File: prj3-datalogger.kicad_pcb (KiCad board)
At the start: 2 copper layers, 29 parts, among them J1 Conn_01x04_Pin, J2 Conn_01x04_Pin, J3 Conn_01x09_Pin, J4 Conn_02x03_Odd_Even, U1 24LC1025, U2 24LC1025, U3 DS1337S_, U4 ATMEGA328P-AU, Y1 32.768 KHz, Y2 16 MHz

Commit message: complet placement of comps.
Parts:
- moved J3 93.8 mm to (81.5, 106.7), turned to 90 degrees
- moved Y1 87.6 mm to (75.9, 95.6), turned to 90 degrees
- moved C1 71.6 mm to (92.7, 80.4)
- moved J1 71.5 mm to (109.1, 106.7), turned to 90 degrees
- moved C4 70.3 mm to (91.9, 101.1), turned to -90 degrees
- moved H4 69.1 mm to (75.3, 80.0)
- moved U3 68.9 mm to (84.8, 100.0)
- moved C3 68.6 mm to (97.8, 80.4)
- moved U1 68.2 mm to (84.7, 82.1)
- moved U2 68.0 mm to (84.7, 90.9)
- moved H3 65.3 mm to (75.3, 106.8)
- moved C2 63.1 mm to (102.5, 80.5), turned to 180 degrees
- moved Y2 62.9 mm to (100.3, 86.2)
- moved J2 60.7 mm to (122.0, 94.3)
- moved J4 59.4 mm to (119.4, 85.1)
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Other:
- board outline added: 53.6 x 33 mm

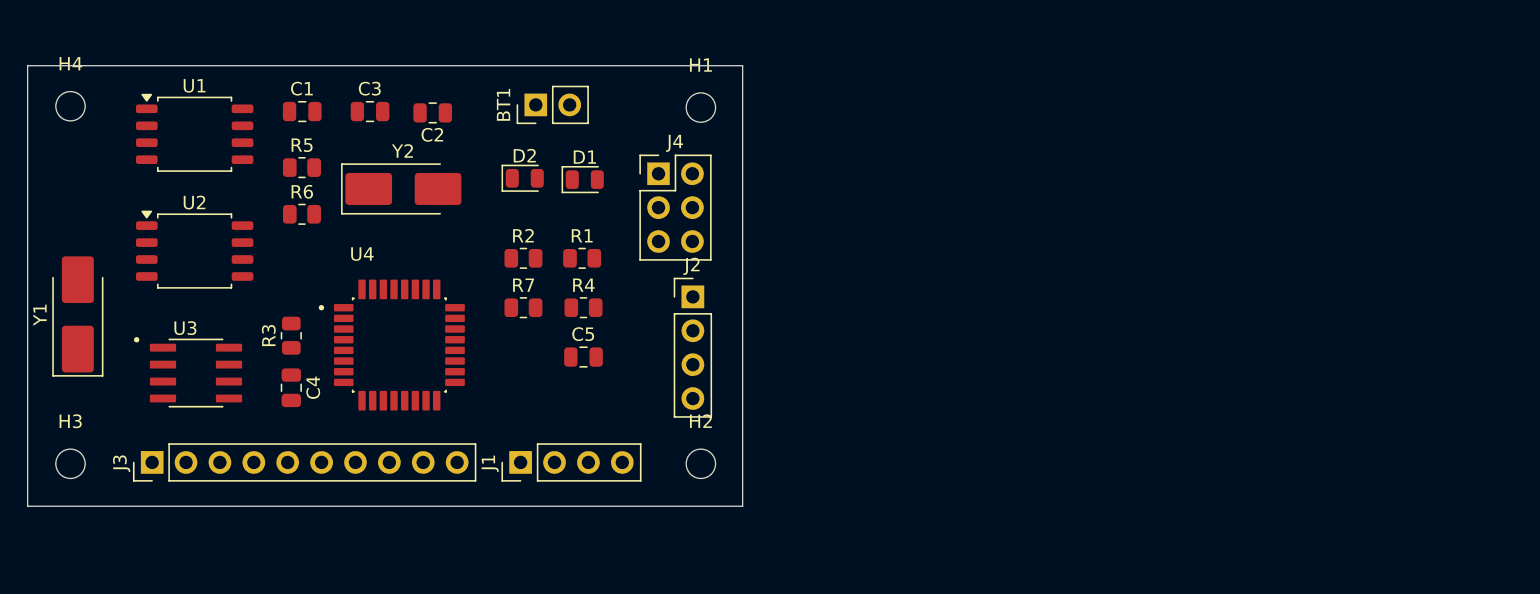
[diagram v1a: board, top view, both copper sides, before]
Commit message: Routing sans GND vcc
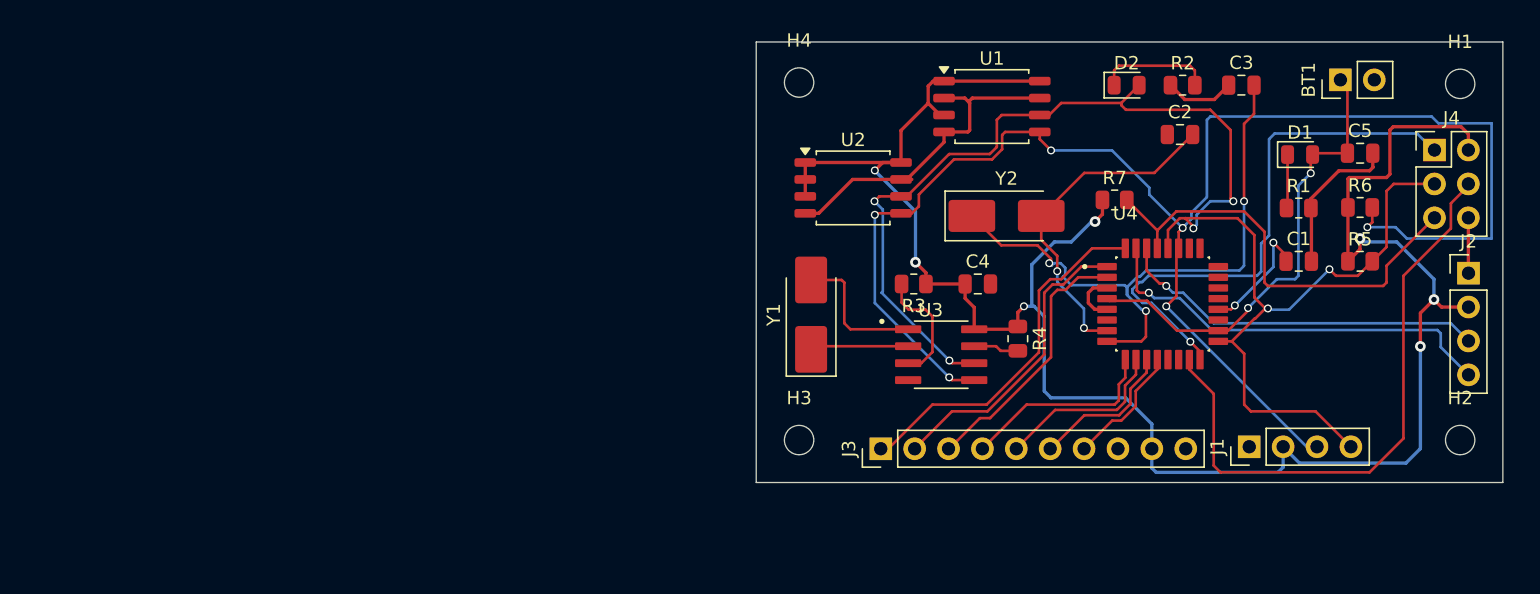
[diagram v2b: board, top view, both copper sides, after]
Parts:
- moved R5 79.6 mm to (172.0, 91.6)
- moved R6 79.3 mm to (172.0, 87.6)
- moved C1 75.5 mm to (167.4, 91.6)
- moved C3 65.3 mm to (163.1, 78.4)
- moved BT1 60.3 mm to (170.5, 78.0)
- moved C5 60.2 mm to (172.0, 83.5)
- moved U1 59.8 mm to (144.4, 80.0)
- moved J4 58.2 mm to (177.6, 83.3)
- moved J2 58.2 mm to (180.1, 92.5)
- moved U4 57.3 mm to (157.2, 94.8)
- moved H1 56.9 mm to (179.5, 78.3)
- moved H2 56.9 mm to (179.5, 105.0)
- moved C2 56.0 mm to (158.5, 82.1), turned to 0 degrees
- moved U3 55.9 mm to (140.6, 98.6)
- moved Y1 55.0 mm to (130.9, 95.6)
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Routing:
- net /VCC: track 0.00 -> 149.9 mm, vias 0 -> 7
- net /SDA: track 0.00 -> 119.6 mm, vias 0 -> 6
- net /SCL: track 0.00 -> 113.9 mm, vias 0 -> 6
- net GND: track 0.00 -> 51.0 mm
- net Net-(U4-PB7): track 0.00 -> 46.4 mm, vias 0 -> 3
- net /MOSI: track 0.00 -> 45.3 mm
- net /MISO: track 0.00 -> 41.4 mm, vias 0 -> 1
- net Net-(BT1-+): track 0.00 -> 35.3 mm, vias 0 -> 2
- net /RESET: track 0.00 -> 33.3 mm
- net /TX: track 0.00 -> 31.3 mm, vias 0 -> 1
- net /RX: track 0.00 -> 28.1 mm, vias 0 -> 1
- net /D2: track 0.00 -> 27.3 mm
- net Net-(U4-PB6): track 0.00 -> 25.4 mm, vias 0 -> 2
- net /D3: track 0.00 -> 22.8 mm
- net /D4: track 0.00 -> 19.9 mm
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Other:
- board size 53.6 x 33 mm -> 56 x 33 mm

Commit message: Routing completed
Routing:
- net GND: track 51.0 -> 92.9 mm, vias 0 -> 10
- net /VCC: track 149.9 -> 152.1 mm, vias 7 -> 9
- net Net-(U4-AREF): track 9.06 -> 7.76 mm
- net /SDA: track 119.6 -> 119.1 mm
- added copper zone on F.Cu, net /VCC
- added copper zone on B.Cu, net GND

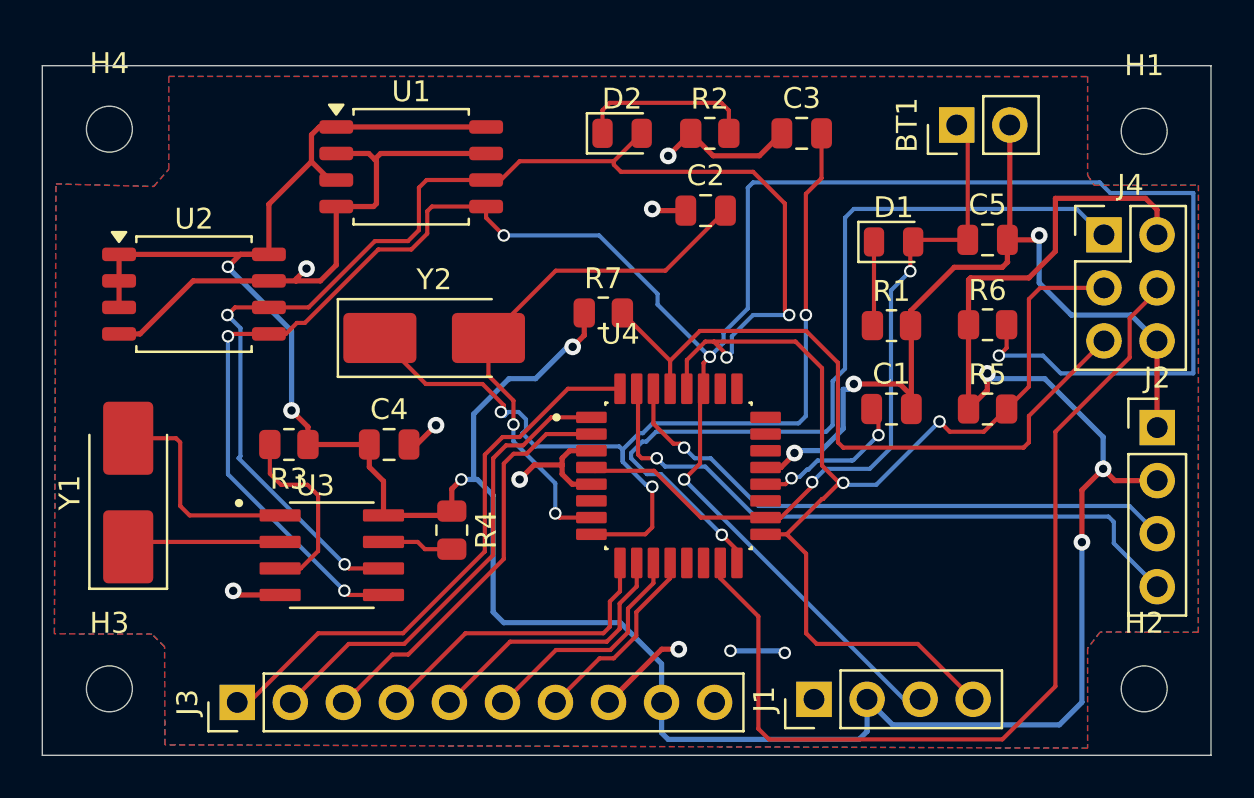
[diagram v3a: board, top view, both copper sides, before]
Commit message: text amends and Vcc label at batt schem
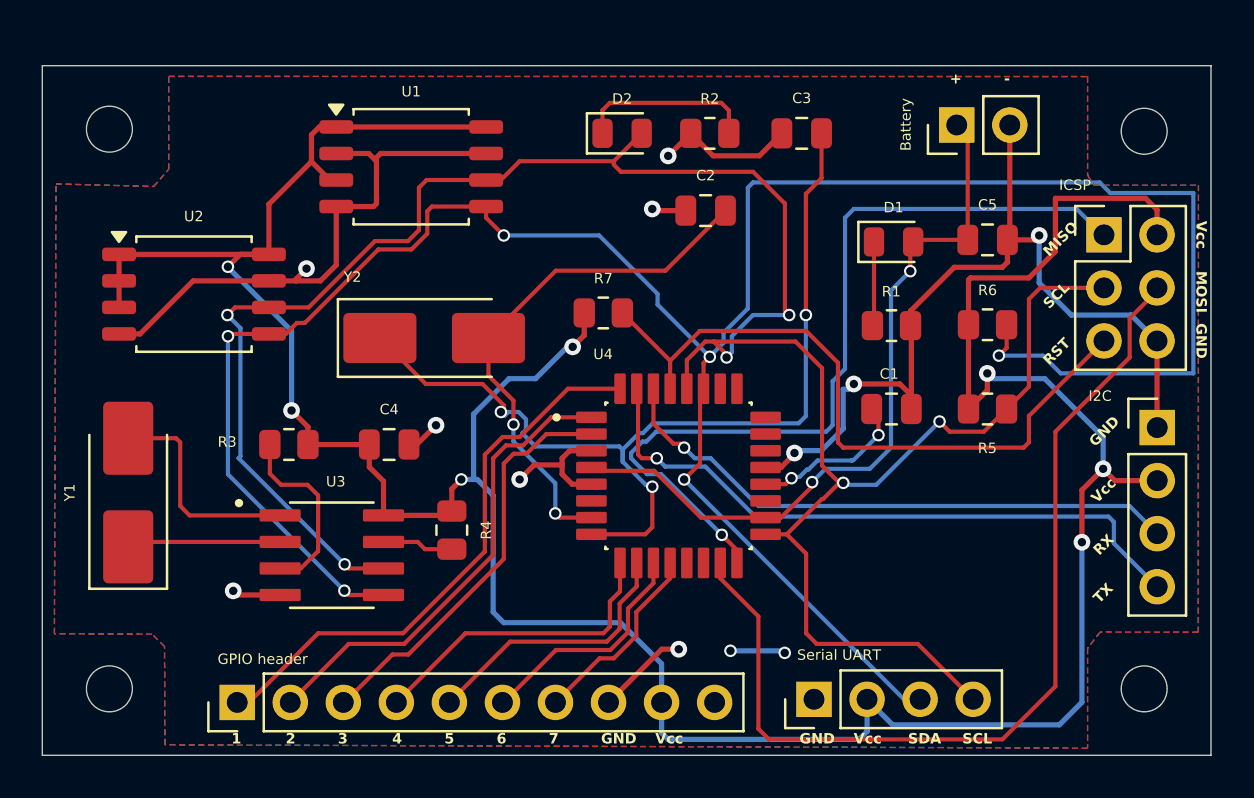
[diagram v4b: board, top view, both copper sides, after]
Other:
- board text added: "+"
- board text added: "-"
- board text added: "1"
- board text added: "2"
- board text added: "3"
- board text added: "4"
- board text added: "5"
- board text added: "6"
- board text added: "7"
- board text added: "GND"
- board text added: "MISO"
- board text added: "MOSI"
- board text added: "RST"
- board text added: "RX"
- board text added: "SCL"
- board text added: "SDA"
- board text added: "TX"
- board text added: "Vcc"
